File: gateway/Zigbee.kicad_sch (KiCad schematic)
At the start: 44 parts, among them IC1001 TXU0102, IC1002 MIC5317-3.3xM5, IC1003 CC2530F128RHAR, Q1001 BSS123, X1001 Conn_Coaxial, Y1001 32MHz, Y1002 32kHz

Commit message: Working on version 1.0
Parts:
- added R1006, R1007: 0R, Resistor_SMD:R_0805_2012Metric, symbol Device:R
- added TP1004, TP1005, TP1006: ~, Testpoints_Kampi:TestPoint_Pad_1.0x1.0mm, symbol Connector:TestPoint
- C1001: renamed from C1005; footprint (none) -> Capacitor_SMD:C_0805_2012Metric; manf (none) -> KYOCERA AVX; manf# (none) -> 08056C105MAT2A; mouser# (none) -> 581-08056C105MAT2A
- C1002: renamed from C1009; footprint (none) -> Capacitor_SMD:C_0805_2012Metric; manf (none) -> KYOCERA AVX; manf# (none) -> 08056C105MAT2A; mouser# (none) -> 581-08056C105MAT2A
- C1003: renamed from C1001; footprint Capacitor_SMD:C_0402_1005Metric -> Capacitor_SMD:C_0805_2012Metric; manf# 04025C104JAT2A -> 08053C104M4T4A; mouser# 581-04025C104JAT2A -> 581-08053C104M4T4A
- C1004: renamed from C1002; footprint Capacitor_SMD:C_0402_1005Metric -> Capacitor_SMD:C_0805_2012Metric; manf# 04025C104JAT2A -> 08053C104M4T4A; mouser# 581-04025C104JAT2A -> 581-08053C104M4T4A
- C1005: renamed from C1003; footprint Capacitor_SMD:C_0402_1005Metric -> Capacitor_SMD:C_0805_2012Metric; manf (none) -> KYOCERA AVX; manf# (none) -> 08051A270KAT2A; mouser# (none) -> 581-08051A270KAT2A
- C1006: renamed from C1004; footprint Capacitor_SMD:C_0402_1005Metric -> Capacitor_SMD:C_0805_2012Metric; manf (none) -> KYOCERA AVX; manf# (none) -> 08051A270KAT2A; mouser# (none) -> 581-08051A270KAT2A
- C1007: renamed from C1006; footprint Capacitor_SMD:C_0402_1005Metric -> Capacitor_SMD:C_0805_2012Metric; manf# 04025C104JAT2A -> 08053C104M4T4A; mouser# (none) -> 581-08053C104M4T4A
- C1008: renamed from C1007; footprint Capacitor_SMD:C_0402_1005Metric -> Capacitor_SMD:C_0805_2012Metric; manf# 04025C104JAT2A -> 08053C104M4T4A; mouser# (none) -> 581-08053C104M4T4A
- C1009: renamed from C1008; footprint Capacitor_SMD:C_0402_1005Metric -> Capacitor_SMD:C_0805_2012Metric; manf# 04025C104JAT2A -> 08053C104M4T4A; mouser# (none) -> 581-08053C104M4T4A
- C1010, C1012, C1013, C1017, C1022, C1023: footprint Capacitor_SMD:C_0402_1005Metric -> Capacitor_SMD:C_0805_2012Metric; manf# 04025C104JAT2A -> 08053C104M4T4A; mouser# (none) -> 581-08053C104M4T4A
- C1011: footprint Capacitor_SMD:C_0402_1005Metric -> Capacitor_SMD:C_0805_2012Metric; manf (none) -> KYOCERA AVX; manf# (none) -> 08056C105MAT2A; mouser# (none) -> 581-08056C105MAT2A
- C1014, C1015, C1016, C1018, C1021: footprint Capacitor_SMD:C_0402_1005Metric -> Capacitor_SMD:C_0805_2012Metric
- C1019, C1020: footprint Capacitor_SMD:C_0402_1005Metric -> Capacitor_SMD:C_0805_2012Metric; manf (none) -> KYOCERA AVX; manf# (none) -> 08052U150JAT2A; mouser# (none) -> 581-08052U150JAT2A
- IC1001: renamed from IC1002; manf (none) -> Microchip Technology; manf# (none) -> MIC5317-3.3YM5-TR; mouser# (none) -> 998-MIC5317-3.3YM5-TR
- R1001: renamed from R1004; footprint (none) -> Resistor_SMD:R_0805_2012Metric; manf (none) -> Bourns; manf# (none) -> CR0805-FX-1002GLF; mouser# (none) -> 652-CR0805-FX-1002GLF
- R1004: renamed from R1003; footprint (none) -> Resistor_SMD:R_0805_2012Metric; manf (none) -> Bourns; manf# (none) -> CR0805-JW-103GLF; mouser# (none) -> 652-CR0805-JW-103GLF
- R1005: renamed from R1007; manf# CR0402-JW-680GLF -> CR0805-JW-680GLF; mouser# 652-CR0402-JW-680GLF -> 652-CR0805-JW-680GLF
- R1008: renamed from R1005; footprint (none) -> Resistor_SMD:R_0805_2012Metric; manf (none) -> Bourns; manf# (none) -> CR0805-JW-103GLF; mouser# (none) -> 652-CR0805-JW-103GLF
- R1009: renamed from R1006; footprint (none) -> Resistor_SMD:R_0805_2012Metric; manf (none) -> Bourns; manf# (none) -> CR0805-FX-5602GLF; mouser# (none) -> 652-CR0805-FX-5602GLF
- TP1001: renamed from TP1003; footprint (none) -> Testpoints_Kampi:TestPoint_Pad_1.0x1.0mm
- TP1002: renamed from TP1001; footprint (none) -> Testpoints_Kampi:TestPoint_Pad_1.0x1.0mm
- TP1003: renamed from TP1002; footprint (none) -> Testpoints_Kampi:TestPoint_Pad_1.0x1.0mm
- X1001: value Conn_Coaxial -> Zigbee; footprint (none) -> Amphenol:A-1JB; manf (none) -> Amphenol RF; manf# (none) -> A-1JB; mouser# (none) -> 523-A-1JB
- renumbered IC1001 to IC1002, R1001 to R1002, R1002 to R1003
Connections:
- net at IC1003.16 (P0_3): now also R1007.2, TP1006.1; no longer IC1002.8 (B1)
- net at IC1003.17 (P0_2): now also R1006.2, TP1005.1; no longer IC1002.1 (B2)
- net at IC1003.20 (~{RESET}), Q1001.3 (D), R1008.2: now also TP1004.1
- net Zigbee-Reset renamed Zigbee.Reset
- net Zigbee-RxD renamed Zigbee.TxD
- net Zigbee-TxD renamed Zigbee.RxD
- new net: IC1002.8 (B1), R1006.1
- new net: IC1002.1 (B2), R1007.1
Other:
- moved on the sheet: C1002, C1004, C1018, L1001, LED1001, Q1001, R1004, R1005, TP1002, TP1003

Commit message: Working on PCB
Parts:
- added MP1001: (no value), Bivar:SLP3-300-100-F, symbol Mechanical_Kampi:Light_Pipe
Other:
- moved on the sheet: C1007, C1008, C1009, C1010, C1012, C1013, C1017, C1022, C1023

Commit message: Working on version 1.0.0
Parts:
- removed C1003, C1004: 100n, Capacitor_SMD:C_0805_2012Metric, symbol Device:C
- removed IC1002: TXU0102, Package_SO:VSSOP-8_2.3x2mm_P0.5mm, symbol Texas Instruments:TXU0102
- added C1026, C1027: 100n, Capacitor_SMD:C_0805_2012Metric, symbol Device:C
- added IC1005: TXB0104RUT, Package_DFN_QFN:Texas_R-PUQFN-N12, symbol Logic_LevelTranslator:TXB0104RUT
- added R1011, R1012: 0R, Resistor_SMD:R_0805_2012Metric, symbol Device:R
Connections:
- net +1V8: now also C1027.1, IC1005.1 (VCCA), IC1005.12 (OE)
- net AVDD: now also C1026.1, IC1005.11 (VCCB)
- net GND: now also C1026.2, C1027.2, IC1005.6 (GND)
- net at R1006.1: now also IC1005.2 (A1)
- net at R1003.2: now also IC1005.9 (B2)
- net at R1007.1: now also IC1005.3 (A2)
- net at R1002.2: now also IC1005.10 (B1)
- new net: IC1005.7 (B4), R1012.2
- new net: IC1005.8 (B3), R1011.2
- new net Zigbee.CTS: R1012.1
- new net Zigbee.RTS: R1011.1
- no-connect marks 18 -> 20
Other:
- moved on the sheet: R1002, R1003

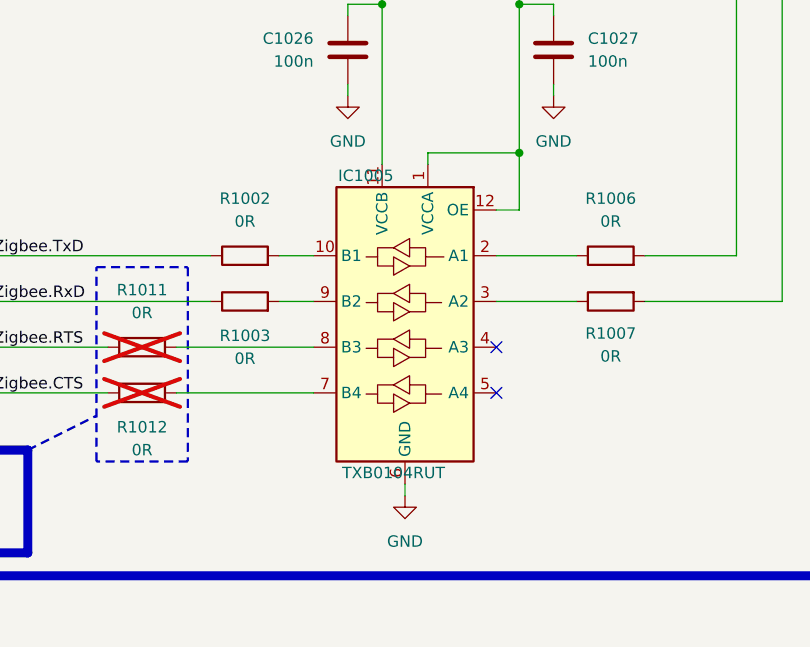
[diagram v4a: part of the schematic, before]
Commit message: Adding level shifter, update documentation
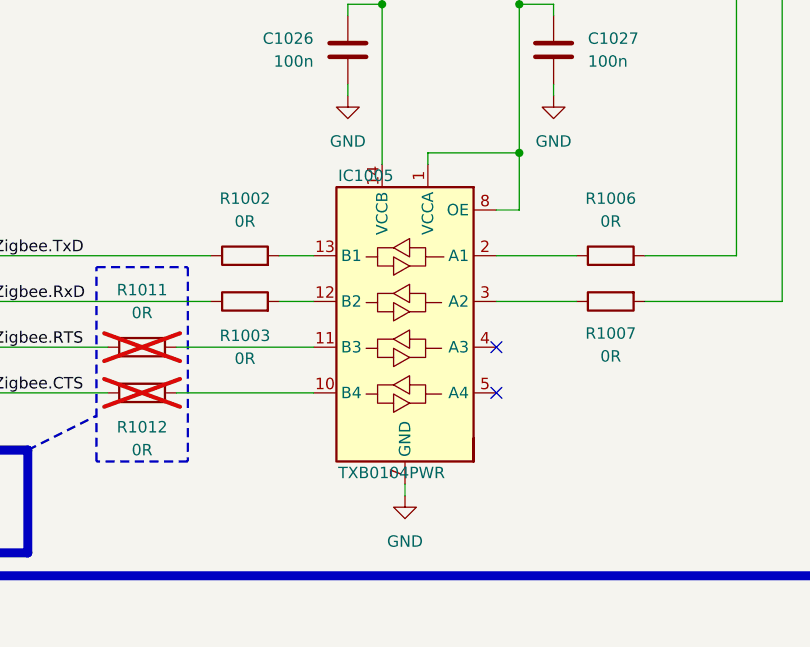
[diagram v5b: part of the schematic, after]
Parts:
- IC1005: value TXB0104RUT -> TXB0104PWR; footprint Package_DFN_QFN:Texas_R-PUQFN-N12 -> Package_SO:TSSOP-14_4.4x5mm_P0.65mm; symbol Logic_LevelTranslator:TXB0104RUT -> Logic_LevelTranslator:TXB0104PW; manf# TXB0104RUTR -> TXB0104PWR; mouser# 595-TXB0104RUTR -> 595-TXB0104PWR
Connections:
- net +1V8: now also IC1005.8 (OE); no longer IC1005.12 (OE)
- net AVDD: now also IC1005.14 (VCCB); no longer IC1005.11 (VCCB)
- net GND: now also IC1005.7 (GND); no longer IC1005.6 (GND)
- net at IC1005.10 (B4): now also R1012.2; no longer R1002.2
- net at R1011.2: now also IC1005.11 (B3); no longer IC1005.8 (B3)
- net at R1003.2: now also IC1005.12 (B2); no longer IC1005.9 (B2)
- new net: IC1005.13 (B1), R1002.2
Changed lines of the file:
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@@
 	)
 	(symbol
-		(lib_id "Logic_LevelTranslator:TXB0104RUT")
+		(lib_id "Logic_LevelTranslator:TXB0104PW")
 		(at 105.41 176.53 0)
 		(mirror y)
@@
 			)
 		)
-		(property "Value" "TXB0104RUT"
+		(property "Value" "TXB0104PWR"
 			(at 109.855 193.04 0)
 			(show_name no)
@@
 			)
 		)
-		(property "Footprint" "Package_DFN_QFN:Texas_R-PUQFN-N12"
+		(property "Footprint" "Package_SO:TSSOP-14_4.4x5mm_P0.65mm"
 			(at 105.41 195.58 0)
 			(hide yes)
@@
 			)
 		)
-		(property "Description" "4-Bit Bidirectional Voltage-Level Translator, Auto Direction Sensing and ±15-kV ESD Protection, 1.2 - 3.6V APort, 1.65 - 5.5V BPort, Texas_PUQFN-12"
+		(property "Description" "4-Bit Bidirectional Voltage-Level Translator, Auto Direction Sensing and ±15-kV ESD Protection, 1.2 - 3.6V APort, 1.65 - 5.5V BPort, TSSOP-14"
 			(at 105.41 176.53 0)
 			(hide yes)
@@
 			)
 		)
-		(property "manf#" "TXB0104RUTR"
+		(property "manf#" "TXB0104PWR"
 			(at 105.41 176.53 0)
 			(hide yes)
@@
 			)
 		)
-		(property "mouser#" "595-TXB0104RUTR"
+		(property "mouser#" "595-TXB0104PWR"
 			(at 105.41 176.53 0)
 			(hide yes)
@@
 		(pin "8"
 		)
+		(pin "13"
+		)
+		(pin "14"
+		)
 		(instances

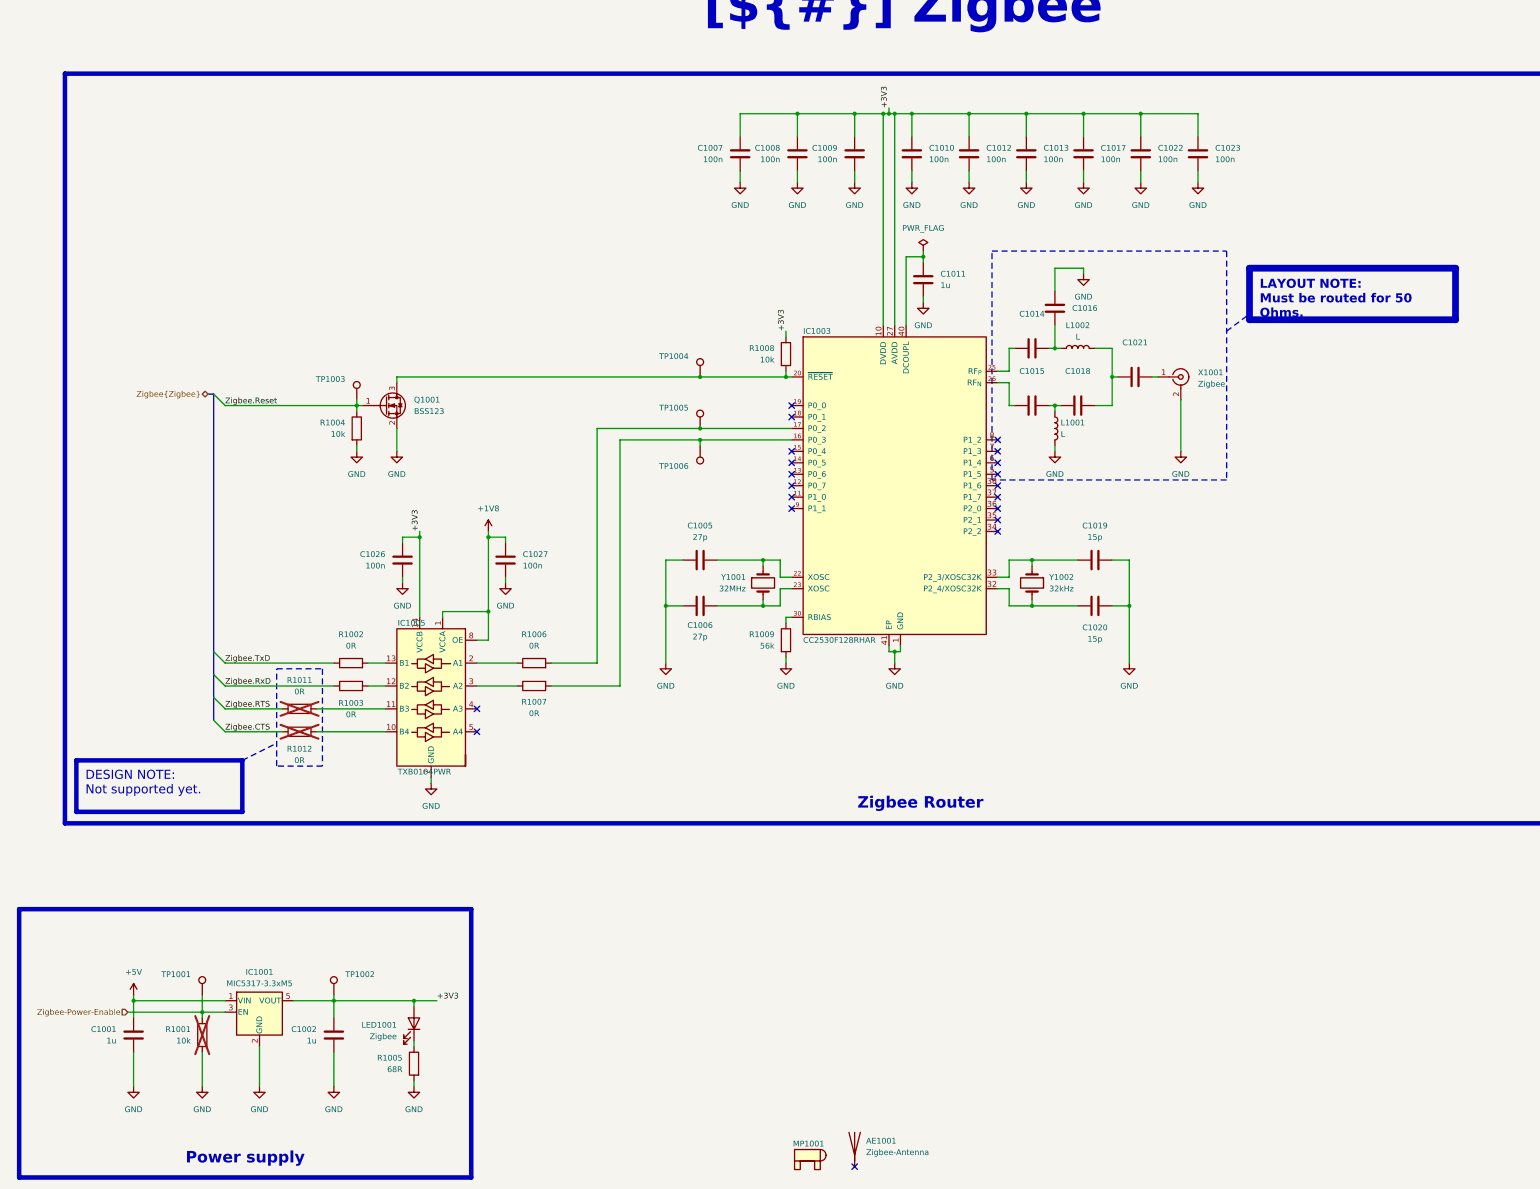
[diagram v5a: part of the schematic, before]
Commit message: Replace level shifter, replace CC2530 with CC2652, fix wrong part numbers
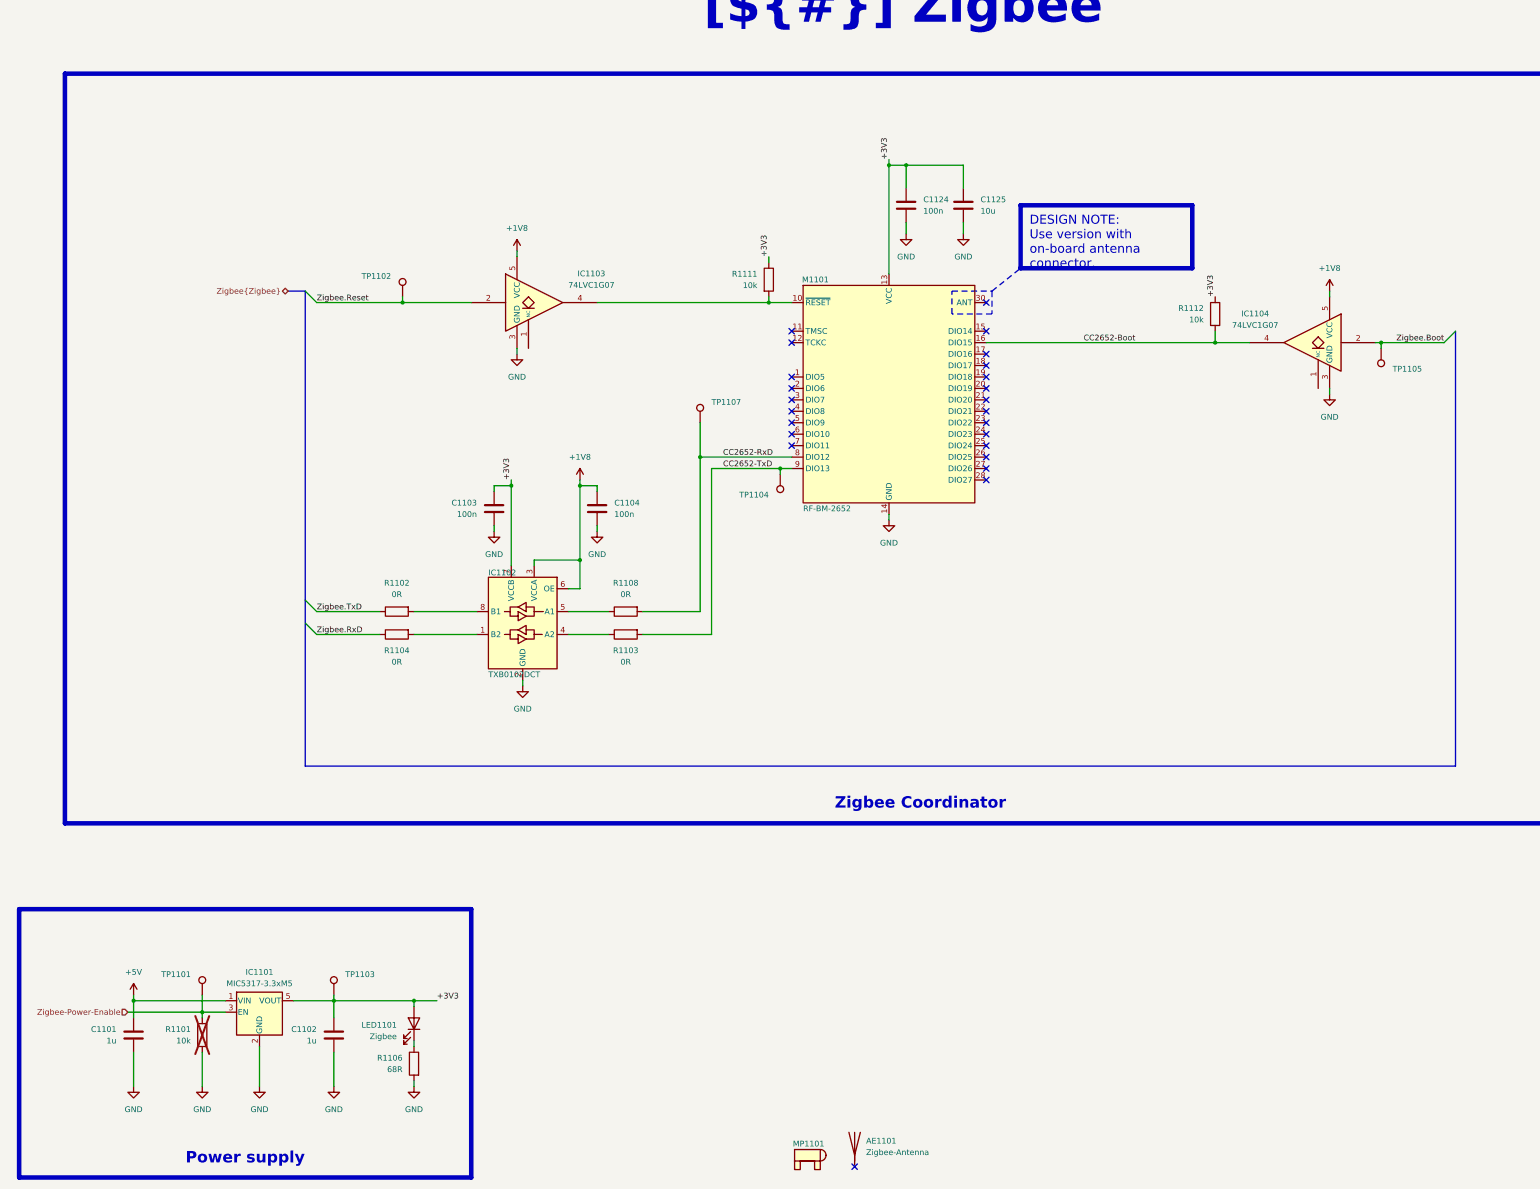
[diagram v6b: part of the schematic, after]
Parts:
- removed AE1001: Zigbee-Antenna, symbol Device:Antenna
- removed C1001, C1002, C1011: 1u, Capacitor_SMD:C_0805_2012Metric, symbol Device:C
- removed C1005, C1006: 27p, Capacitor_SMD:C_0805_2012Metric, symbol Device:C
- removed C1007, C1008, C1009, C1010, C1012, C1013, C1017, C1022, C1023: 100n, Capacitor_SMD:C_0805_2012Metric, symbol Device:C
- removed C1014, C1015, C1016, C1018, C1021: (no value), Capacitor_SMD:C_0805_2012Metric, symbol Device:C
- removed C1019, C1020: 15p, Capacitor_SMD:C_0805_2012Metric, symbol Device:C
- removed IC1001: MIC5317-3.3xM5, Package_TO_SOT_SMD:SOT-23-5, symbol Regulator_Linear:MIC5317-3.3xM5
- removed IC1003: CC2530F128RHAR, Package_DFN_QFN:VQFN-40-1EP_6x6mm_P0.5mm_EP3.5x3.5mm_ThermalVias, symbol Texas Instruments:CC2530
- removed L1001, L1002: L, symbol Device:L
- removed LED1001: Zigbee, LED_SMD:LED_0805_2012Metric, symbol Device:LED
- removed MP1001: (no value), Bivar:SLP3-300-100-F, symbol Mechanical_Kampi:Light_Pipe
- removed Q1001: BSS123, Package_TO_SOT_SMD:SOT-23, symbol Transistor_FET:BSS123
- removed R1001, R1004, R1008: 10k, Resistor_SMD:R_0805_2012Metric, symbol Device:R
- removed R1002, R1003, R1006, R1011, R1012: 0R, Resistor_SMD:R_0805_2012Metric, symbol Device:R
- removed R1005: 68R, Resistor_SMD:R_0402_1005Metric, symbol Device:R
- removed R1009: 56k, Resistor_SMD:R_0805_2012Metric, symbol Device:R
- removed TP1001, TP1002, TP1004, TP1005, TP1006: ~, Testpoints_Kampi:TestPoint_Pad_1.0x1.0mm, symbol Connector:TestPoint
- removed X1001: Zigbee, Amphenol:A-1JB, symbol Connector:Conn_Coaxial
- removed Y1001: 32MHz, Crystal:Crystal_SMD_Abracon_ABM7-2Pin_6.0x3.5mm, symbol Device:Crystal
- removed Y1002: 32kHz, Abracon:ABS07, symbol Device:Crystal
- added AE1101: Zigbee-Antenna, symbol Device:Antenna
- added C1101, C1102: 1u, Capacitor_SMD:C_0805_2012Metric, symbol Device:C
- added C1124: 100n, Capacitor_SMD:C_0805_2012Metric, symbol Device:C
- added C1125: 10u, Capacitor_SMD:C_0805_2012Metric, symbol Device:C
- added IC1101: MIC5317-3.3xM5, Package_TO_SOT_SMD:SOT-23-5, symbol Regulator_Linear:MIC5317-3.3xM5
- added IC1103, IC1104: 74LVC1G07, Package_TO_SOT_SMD:SOT-353_SC-70-5, symbol 74xGxx:74LVC1G07
- added LED1101: Zigbee, LED_SMD:LED_0805_2012Metric, symbol Device:LED
- added M1101: RF-BM-2652, Rf-star:RF-BM-2652, symbol Rf-star:RF-BM-2652
- added MP1101: (no value), Bivar:SLP3-300-100-F, symbol Mechanical_Kampi:Light_Pipe
- added R1101, R1111, R1112: 10k, Resistor_SMD:R_0805_2012Metric, symbol Device:R
- added R1102, R1103, R1104: 0R, Resistor_SMD:R_0805_2012Metric, symbol Device:R
- added R1106: 68R, Resistor_SMD:R_0805_2012Metric, symbol Device:R
- added TP1101, TP1103, TP1104, TP1105, TP1107: ~, Testpoints_Kampi:TestPoint_Pad_1.0x1.0mm, symbol Connector:TestPoint
- IC1102: renamed from IC1005; value TXB0104PWR -> TXB0102DCT; footprint Package_SO:TSSOP-14_4.4x5mm_P0.65mm -> Package_SO:VSSOP-8_2.3x2mm_P0.5mm; symbol Logic_LevelTranslator:TXB0104PW -> Logic_LevelTranslator:TXB0102DCT; manf# TXB0104PWR -> TXB0102DCT; mouser# 595-TXB0104PWR -> 595-TXB0102DCT
- renumbered C1026 to C1103, C1027 to C1104, R1007 to R1108, TP1003 to TP1102
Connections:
- net +1V8: now also IC1102.3 (VCCA), IC1102.6 (OE), IC1103.5 (VCC), IC1104.5 (VCC); no longer IC1102.1 (VCCA), IC1102.8 (OE)
- net +5V: now also C1101.2, IC1101.1 (VIN)
- net GND: now also IC1102.2 (GND), C1101.1, C1102.1, C1124.1, C1125.2, IC1101.2 (GND), IC1103.3 (GND), IC1104.3 (GND), M1101.14 (GND), M1101.29 (GND), R1101.2, R1106.2; no longer IC1102.7 (GND)
- net Zigbee-Power-Enable: now also IC1101.3 (EN), R1101.1, TP1101.1
- net Zigbee.Reset: now also IC1103.2
- net Zigbee.RxD: now also R1104.1
- net Zigbee.TxD: now also R1102.1
- net at R1108.1: now also IC1102.5 (A1); no longer IC1102.3 (A2)
- net at IC1102.4 (A2): now also R1103.1
- net CC2652-RxD: now reaches R1108.2
- net CC2652-RxD: now also M1101.8 (DIO12), TP1107.1
- net AVDD renamed +3V3
- net +3V3: now also IC1102.7 (VCCB), C1102.2, C1124.2, C1125.1, IC1101.5 (VOUT), LED1101.2 (A), M1101.13 (VCC), R1111.1, R1112.1, TP1103.1; no longer IC1102.14 (VCCB)
- new net: IC1103.4, M1101.10 (~{RESET}), R1111.2
- new net: IC1102.1 (B2), R1104.2
- new net: IC1102.8 (B1), R1102.2
- new net: LED1101.1 (K), R1106.1
- new net CC2652-Boot: IC1104.4, M1101.16 (DIO15), R1112.2
- new net CC2652-TxD: M1101.9 (DIO13), R1103.2, TP1104.1
- new net Zigbee.Boot: IC1104.2, TP1105.1
- no-connect marks 20 -> 24
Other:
- moved on the sheet: C1103, C1104, R1108, TP1102
